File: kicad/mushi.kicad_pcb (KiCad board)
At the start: 2 copper layers, 261 x 90.8 mm, 86 parts

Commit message: cleanup
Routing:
- net GND: track 557.1 -> 555.9 mm
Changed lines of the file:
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@@
   (segment (start 111.094241 84.630759) (end 103.29942 84.630759) (width 0.25) (layer "B.Cu") (net 2))
   (segment (start 112.49945 58.285787) (end 112.49945 66.85055) (width 0.25) (layer "B.Cu") (net 2))
-  (segment (start 94.629074 54.259667) (end 94.629074 47.754074) (width 0.25) (layer "B.Cu") (net 2))
   (segment (start 94.035782 64.410782) (end 93.239995 63.614995) (width 0.25) (layer "B.Cu") (net 2))
   (segment (start 37.916677 70.016677) (end 36.842239 68.942239) (width 0.25) (layer "B.Cu") (net 2))
@@
   (segment (start 36.435029 58.607746) (end 36.435029 52.785029) (width 0.25) (layer "B.Cu") (net 2))
   (segment (start 94.629074 47.754074) (end 93.500351 46.625351) (width 0.25) (layer "B.Cu") (net 2))
+  (segment (start 95.227603 50.651471) (end 94.629074 51.25) (width 0.25) (layer "B.Cu") (net 2))
   (segment (start 36.435029 52.785029) (end 35.656929 52.006929) (width 0.25) (layer "B.Cu") (net 2))
+  (segment (start 104.486003 50.651471) (end 95.227603 50.651471) (width 0.25) (layer "B.Cu") (net 2))
   (segment (start 57.70995 51.918233) (end 57.70995 45.53495) (width 0.25) (layer "B.Cu") (net 2))
   (segment (start 107.48438 94.74029) (end 107.48438 103.34062) (width 0.25) (layer "B.Cu") (net 2))
-  (segment (start 104.486003 50.651471) (end 98.23727 50.651471) (width 0.25) (layer "B.Cu") (net 2))
+  (segment (start 94.629074 54.259667) (end 94.629074 51.25) (width 0.25) (layer "B.Cu") (net 2))
   (segment (start 111.906159 75.275431) (end 111.906159 67.838389) (width 0.25) (layer "B.Cu") (net 2))
   (segment (start 111.906159 75.275431) (end 111.906159 77.755802) (width 0.25) (layer "B.Cu") (net 2))
@@
   (segment (start 75.70995 29.308233) (end 75.70995 38.19005) (width 0.25) (layer "B.Cu") (net 2))
   (segment (start 118.975 105.725) (end 128.125 105.725) (width 0.25) (layer "B.Cu") (net 2))
-  (segment (start 98.23727 50.651471) (end 94.629074 54.259667) (width 0.25) (layer "B.Cu") (net 2))
   (segment (start 84.201249 106.423751) (end 83.37338 107.25162) (width 0.25) (layer "B.Cu") (net 2))
   (segment (start 74.958233 55.958233) (end 67.43495 55.958233) (width 0.25) (layer "B.Cu") (net 2))
@@
   (segment (start 56.918233 61.568233) (end 49.43495 61.568233) (width 0.25) (layer "B.Cu") (net 2))
   (segment (start 126.73495 81.458233) (end 112.983233 81.458233) (width 0.25) (layer "B.Cu") (net 2))
+  (segment (start 94.629074 51.25) (end 94.629074 47.754074) (width 0.25) (layer "B.Cu") (net 2))
   (segment (start 56.856767 61.568233) (end 49.43495 61.568233) (width 0.25) (layer "B.Cu") (net 2))
   (segment (start 84.201249 95.516809) (end 95.087299 84.630759) (width 0.25) (layer "B.Cu") (net 2))

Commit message: cleanup
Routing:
- net GND: track 555.9 -> 561.7 mm
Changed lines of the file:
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@@
   (segment (start 94.035782 79.814218) (end 93.245361 80.604639) (width 0.25) (layer "B.Cu") (net 2))
   (segment (start 84.955631 104.095618) (end 84.201249 104.85) (width 0.25) (layer "B.Cu") (net 2))
+  (segment (start 84.201249 85.648751) (end 84.201249 95.516809) (width 0.25) (layer "B.Cu") (net 2))
   (segment (start 86.615626 46.625351) (end 76.027068 46.625351) (width 0.25) (layer "B.Cu") (net 2))
   (segment (start 75.041767 72.958233) (end 67.43495 72.958233) (width 0.25) (layer "B.Cu") (net 2))
@@
   (segment (start 112.49945 58.285787) (end 112.120319 58.285787) (width 0.25) (layer "B.Cu") (net 2))
   (segment (start 75.70995 72.29005) (end 75.041767 72.958233) (width 0.25) (layer "B.Cu") (net 2))
+  (segment (start 85.219241 84.630759) (end 84.201249 85.648751) (width 0.25) (layer "B.Cu") (net 2))
   (segment (start 94.629074 62.270926) (end 93.285005 63.614995) (width 0.25) (layer "B.Cu") (net 2))
   (segment (start 98.877641 104.095618) (end 111.695618 104.095618) (width 0.25) (layer "B.Cu") (net 2))
-  (segment (start 95.087299 84.630759) (end 103.29942 84.630759) (width 0.25) (layer "B.Cu") (net 2))
   (segment (start 67.43495 38.958233) (end 58.476717 38.958233) (width 0.25) (layer "B.Cu") (net 2))
   (segment (start 94.524649 46.625351) (end 88.347408 46.625351) (width 0.25) (layer "B.Cu") (net 2))
@@
   (segment (start 94.629074 51.25) (end 94.629074 47.754074) (width 0.25) (layer "B.Cu") (net 2))
   (segment (start 56.856767 61.568233) (end 49.43495 61.568233) (width 0.25) (layer "B.Cu") (net 2))
-  (segment (start 84.201249 95.516809) (end 95.087299 84.630759) (width 0.25) (layer "B.Cu") (net 2))
+  (segment (start 103.29942 84.630759) (end 85.219241 84.630759) (width 0.25) (layer "B.Cu") (net 2))
   (segment (start 94.035782 71.249311) (end 94.035782 79.814218) (width 0.25) (layer "B.Cu") (net 2))
   (segment (start 76.027068 46.625351) (end 75.70995 46.308233) (width 0.25) (layer "B.Cu") (net 2))

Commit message: new zones and logo
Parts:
- removed ? (x2): LOGO, images:mushi
- added G***: LOGO, images:mushi_copper, F.Cu at (67.2, 82.9)
- added G***: LOGO, images:mushi_copper, F.Cu at (225.5, 83.8)
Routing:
- net rGND: track 594.9 -> 0.00 mm
- net GND: track 561.7 -> 0.00 mm
- net mirror_matrix_index_middle: track 51.4 -> 50.6 mm
- net mirror_matrix_index_top: track 55.2 -> 54.5 mm
- net matrix_outer_top: track 44.3 -> 43.6 mm
- net mirror_matrix_outer_bottom: track 36.4 -> 35.8 mm
- net mirror_matrix_outer_top: track 30.5 -> 29.9 mm
- added copper zone on B.Cu, net GND
- added copper zone on B.Cu, net rGND
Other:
- board text added: "© your name rev1"

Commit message: cleanup
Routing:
- net matrix_ring_bottom: track 137.0 -> 135.5 mm
- net mirror_matrix_pinky_bottom: track 148.7 -> 147.1 mm
- net mirror_matrix_pinky_middle: track 132.6 -> 131.1 mm
- net matrix_pinky_middle: track 144.4 -> 142.9 mm
- net matrix_middle_bottom: track 112.9 -> 111.4 mm
- net mirror_matrix_ring_bottom: track 120.2 -> 118.8 mm
- net matrix_ring_middle: track 114.6 -> 113.2 mm
- net matrix_middle_middle: track 96.2 -> 94.8 mm
- net mirror_matrix_pinky_top: track 132.4 -> 131.1 mm
- net mirror_matrix_ring_top: track 101.3 -> 100.0 mm
- net mirror_matrix_ring_middle: track 102.8 -> 101.6 mm
- net mirror_thumbs_inner_cluster: track 109.3 -> 108.1 mm
- net thumbs_outer_cluster: track 67.9 -> 66.7 mm
- net mirror_matrix_middle_bottom: track 90.4 -> 89.2 mm
- net mirror_matrix_middle_top: track 83.0 -> 81.9 mm
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
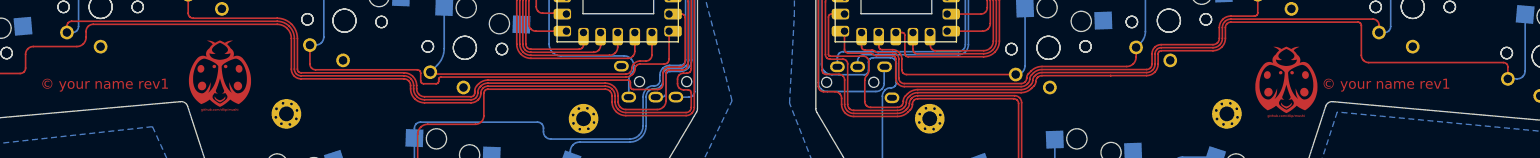
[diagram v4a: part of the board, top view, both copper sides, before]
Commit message: update logos
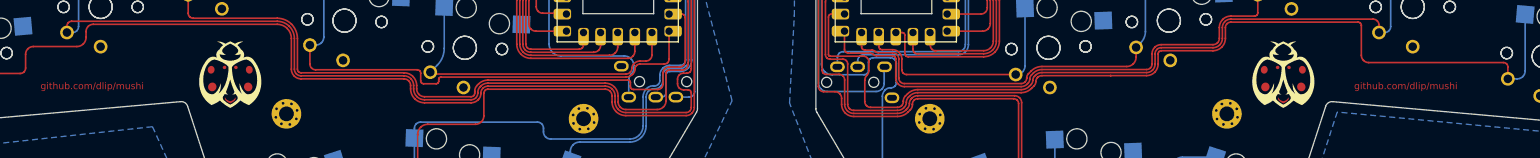
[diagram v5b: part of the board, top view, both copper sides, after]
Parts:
- removed G*** (x2): LOGO, images:mushi_copper
- added ?: LOGO, images:mushi_copper2, F.Cu at (68.7, 83.0)
- added ?: LOGO, images:mushi_copper2, F.Cu at (225.0, 83.0)
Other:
- board text added: "github.com/dlip/mushi"
- board text removed: "© your name rev1"

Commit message: revert track rounding
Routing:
- net matrix_pinky_bottom: track 166.2 -> 168.4 mm
- net matrix_ring_bottom: track 135.5 -> 137.1 mm
- net mirror_matrix_pinky_bottom: track 147.1 -> 148.7 mm
- net mirror_matrix_pinky_middle: track 131.1 -> 132.6 mm
- net matrix_pinky_middle: track 142.9 -> 144.4 mm
- net mirror_matrix_ring_bottom: track 118.8 -> 120.2 mm
- net matrix_ring_middle: track 113.2 -> 114.6 mm
- net matrix_middle_bottom: track 111.4 -> 112.8 mm
- net matrix_middle_middle: track 94.8 -> 96.2 mm
- net matrix_pinky_top: track 141.5 -> 142.9 mm
- net mirror_matrix_pinky_top: track 131.1 -> 132.4 mm
- net thumbs_inner_cluster: track 126.3 -> 127.6 mm
- net mirror_matrix_ring_top: track 100.0 -> 101.3 mm
- net mirror_matrix_ring_middle: track 101.6 -> 102.8 mm
- net matrix_middle_top: track 93.8 -> 95.0 mm
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
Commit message: cleanup
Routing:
- net thumbs_inner_cluster: track 127.6 -> 125.6 mm
- net mirror_matrix_pinky_bottom: track 148.7 -> 147.1 mm
- net mirror_matrix_pinky_middle: track 132.6 -> 131.1 mm
- net matrix_pinky_middle: track 144.4 -> 142.9 mm
- net matrix_pinky_bottom: track 168.4 -> 167.0 mm
- net mirror_matrix_ring_bottom: track 120.2 -> 118.8 mm
- net matrix_ring_middle: track 114.6 -> 113.2 mm
- net matrix_middle_middle: track 96.2 -> 94.8 mm
- net matrix_pinky_top: track 142.9 -> 141.5 mm
- net mirror_matrix_pinky_top: track 132.4 -> 131.1 mm
- net matrix_index_bottom: track 76.4 -> 77.7 mm
- net mirror_matrix_ring_top: track 101.3 -> 100.0 mm
- net mirror_matrix_ring_middle: track 102.8 -> 101.6 mm
- net matrix_middle_top: track 95.0 -> 93.8 mm
- net mirror_thumbs_inner_cluster: track 109.3 -> 108.1 mm
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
